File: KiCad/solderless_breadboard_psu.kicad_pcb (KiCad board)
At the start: 4 copper layers, 55 x 49.8 mm, 87 parts, among them IC301 MCP73831T-2ACI_OT, IC302 BQ29737DSER, IC401 TLV62569DBVR, IC501 FT232RL-REEL, J201 Barrel_Jack_Switch_Pin3Ring, J301 BM02B-GHS-TBT_LF__SN__N_, J501 Conn_01x09_Pin, J502 Conn_01x09_Pin, J503 Conn_01x06_Pin, J504 USB_C_Receptacle_USB2.0_16P, J601 Conn_02x03_Odd_Even, J602 Conn_02x03_Odd_Even, Q301 DMG3415U-7, Q302 T2N7002AK, Q303 T2N7002AK, U401 TPS61040DBVR, U501 USBLC6-2SC6

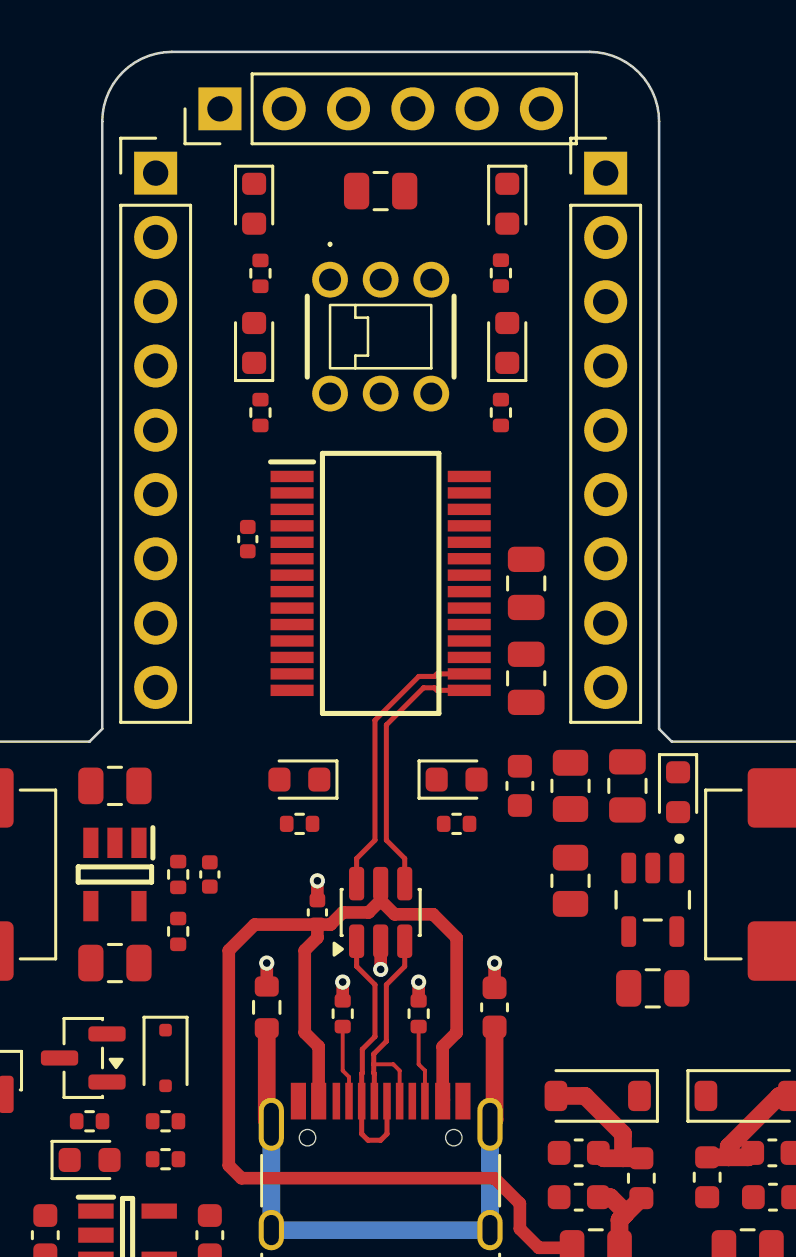
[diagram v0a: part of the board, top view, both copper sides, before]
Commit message: PCB UART routing
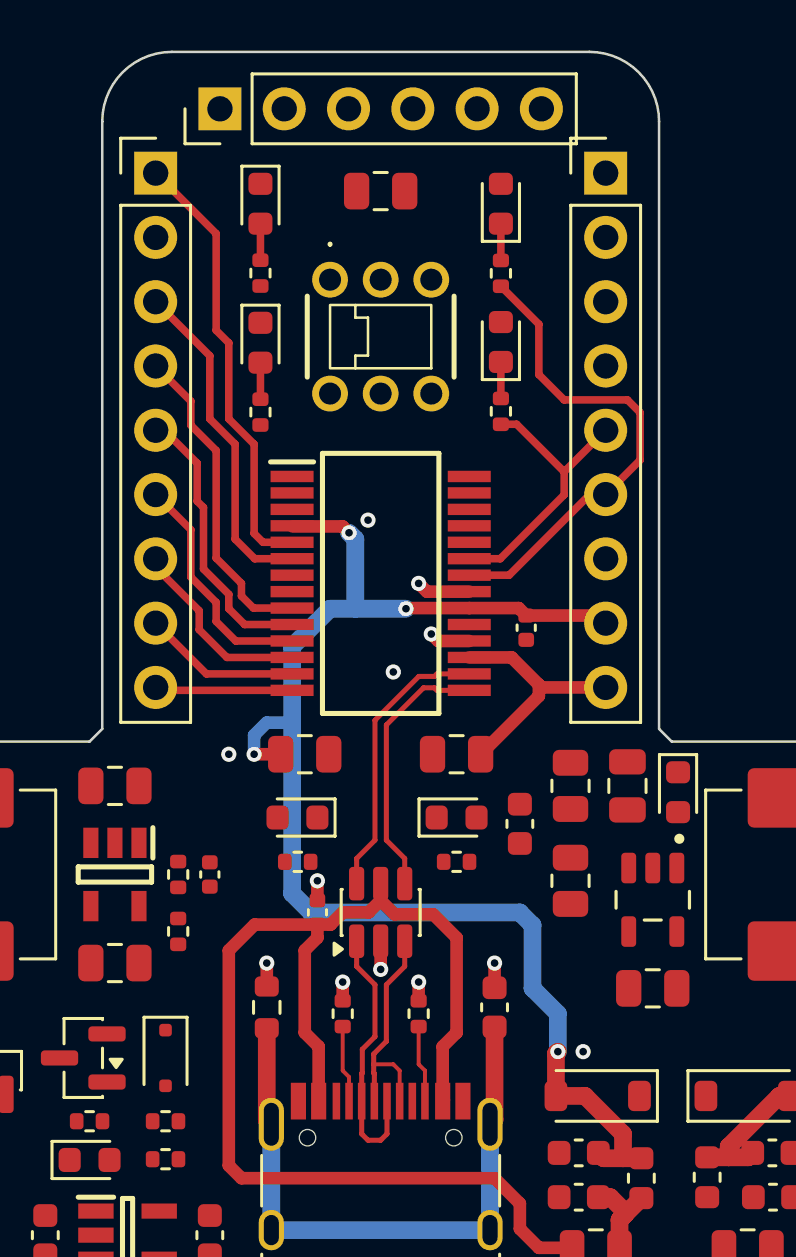
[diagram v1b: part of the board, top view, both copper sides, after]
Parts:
- moved C502 11.5 mm to (55.8, 70.5)
- moved C501 11.1 mm to (47.0, 75.5), turned to 0 degrees
- moved D501 9.75 mm to (54.8, 59.2)
- moved D606 9.75 mm to (45.2, 53.8)
- moved R503 9.50 mm to (54.8, 62.0)
- moved R606 9.50 mm to (45.2, 56.5)
- moved D502 5.51 mm to (54.8, 53.8)
- moved R504 5.50 mm to (54.8, 56.5)
- moved D605 5.50 mm to (45.2, 59.2)
- moved R605 5.48 mm to (45.2, 62.0)
- moved C503 4.07 mm to (53.0, 75.5), turned to 180 degrees
- moved D403 1.50 mm to (46.7, 78.0)
- moved R406 1.50 mm to (46.7, 79.8)
- moved C405 1.50 mm to (55.5, 78.2)
- moved D402 1.50 mm to (53.0, 78.0)
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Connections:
- J501 pad 5: /[5]USB 2 UART/RXD -> /[5]USB 2 UART/RX_LED
- J501 pad 6: /[5]USB 2 UART/RI -> /[5]USB 2 UART/TX_LED
- J501 pad 8: /[5]USB 2 UART/DSR -> +VCC_USB2UART_FILT
- J501 pad 9: /[5]USB 2 UART/DCD -> +3V3_FTDI
- J502 pad 1: /[5]USB 2 UART/RX_LED -> /[5]USB 2 UART/RXD
- J502 pad 3: /[5]USB 2 UART/TX_LED -> /[5]USB 2 UART/RI
- J502 pad 4: +VCC_USB2UART_FILT -> /[5]USB 2 UART/DSR
- J502 pad 5: +3V3_FTDI -> /[5]USB 2 UART/DCD
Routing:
- net +VCC_USB2UART_FILT: track 6.02 -> 55.4 mm, vias 0 -> 4
- net /[5]USB 2 UART/TX_LED: track 0.00 -> 19.2 mm
- net /[5]USB 2 UART/RXD: track 0.00 -> 17.5 mm
- net /[5]USB 2 UART/RI: track 0.00 -> 13.3 mm
- net /[5]USB 2 UART/DSR: track 0.00 -> 12.7 mm
- net /[5]USB 2 UART/RX_LED: track 0.00 -> 11.3 mm
- net /[5]USB 2 UART/DCD: track 0.00 -> 11.2 mm
- net +3V3_FTDI: track 0.00 -> 9.58 mm
- net /[5]USB 2 UART/CTS: track 0.00 -> 9.32 mm
- net /[5]USB 2 UART/SLEEP: track 0.00 -> 8.18 mm
- net /[5]USB 2 UART/TEN: track 0.00 -> 6.22 mm
- net /[5]USB 2 UART/PWREN: track 0.00 -> 5.44 mm
- net GND: track 5.26 -> 9.01 mm, vias 6 -> 12
- net Net-(D502-K): track 0.00 -> 1.45 mm
- net Net-(D501-K): track 0.00 -> 1.44 mm
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
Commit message: Update FTDI pinout
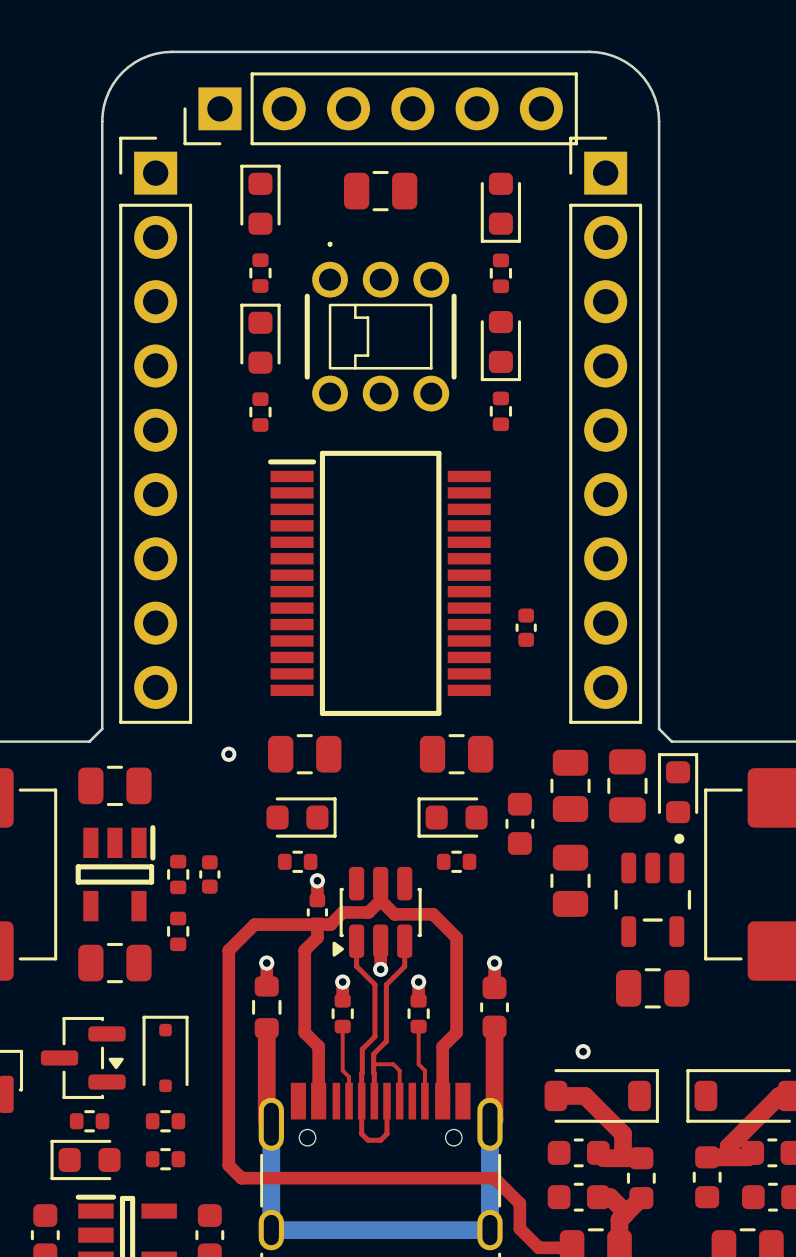
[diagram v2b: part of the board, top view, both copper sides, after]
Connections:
- J501 pad 1: /[5]USB 2 UART/TXD -> GND
- J501 pad 2: /[5]USB 2 UART/DTR -> +VCC_USB2UART_FILT
- J501 pad 3: /[5]USB 2 UART/RTS -> +3V3_FTDI
- J501 pad 4: VCC_FTDI -> GND
- J501 pad 5: /[5]USB 2 UART/RX_LED -> GND
- J501 pad 6: /[5]USB 2 UART/TX_LED -> /[5]USB 2 UART/CTS
- J501 pad 7: GND -> /[5]USB 2 UART/SLEEP
- J501 pad 8: +VCC_USB2UART_FILT -> /[5]USB 2 UART/TEN
- J501 pad 9: +3V3_FTDI -> /[5]USB 2 UART/PWREN
- J502 pad 1: /[5]USB 2 UART/RXD -> /[5]USB 2 UART/TXD
- J502 pad 2: GND -> /[5]USB 2 UART/DTR
- J502 pad 3: /[5]USB 2 UART/RI -> /[5]USB 2 UART/RTS
- J502 pad 4: /[5]USB 2 UART/DSR -> VCC_FTDI
- J502 pad 5: /[5]USB 2 UART/DCD -> /[5]USB 2 UART/RXD
- J502 pad 6: /[5]USB 2 UART/CTS -> /[5]USB 2 UART/RI
- J502 pad 7: /[5]USB 2 UART/SLEEP -> GND
- J502 pad 8: /[5]USB 2 UART/TEN -> /[5]USB 2 UART/DSR
- J502 pad 9: /[5]USB 2 UART/PWREN -> /[5]USB 2 UART/DCD
- J503 pad 1: /[5]USB 2 UART/DTR -> GND
- J503 pad 2: /[5]USB 2 UART/RXD -> /[5]USB 2 UART/CTS
- J503 pad 3: /[5]USB 2 UART/TXD -> VCC_FTDI
- J503 pad 4: VCC_FTDI -> /[5]USB 2 UART/TXD
- J503 pad 5: /[5]USB 2 UART/CTS -> /[5]USB 2 UART/RXD
- J503 pad 6: GND -> /[5]USB 2 UART/DTR
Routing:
- net +VCC_USB2UART_FILT: track 55.4 -> 6.02 mm, vias 4 -> 0
- net /[5]USB 2 UART/TX_LED: track 19.2 -> 0.00 mm
- net /[5]USB 2 UART/RXD: track 17.5 -> 0.00 mm
- net /[5]USB 2 UART/RI: track 13.3 -> 0.00 mm
- net /[5]USB 2 UART/DSR: track 12.7 -> 0.00 mm
- net /[5]USB 2 UART/RX_LED: track 11.3 -> 0.00 mm
- net /[5]USB 2 UART/USB2UART_D-: track 11.2 -> 0.00 mm
- net /[5]USB 2 UART/DCD: track 11.2 -> 0.00 mm
- net /[5]USB 2 UART/USB2UART_D+: track 10.5 -> 0.00 mm
- net +3V3_FTDI: track 9.58 -> 0.00 mm
- net /[5]USB 2 UART/CTS: track 9.32 -> 0.00 mm
- net /[5]USB 2 UART/SLEEP: track 8.18 -> 0.00 mm
- net /[5]USB 2 UART/TEN: track 6.22 -> 0.00 mm
- net /[5]USB 2 UART/PWREN: track 5.44 -> 0.00 mm
- net GND: track 9.01 -> 5.26 mm, vias 12 -> 8
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
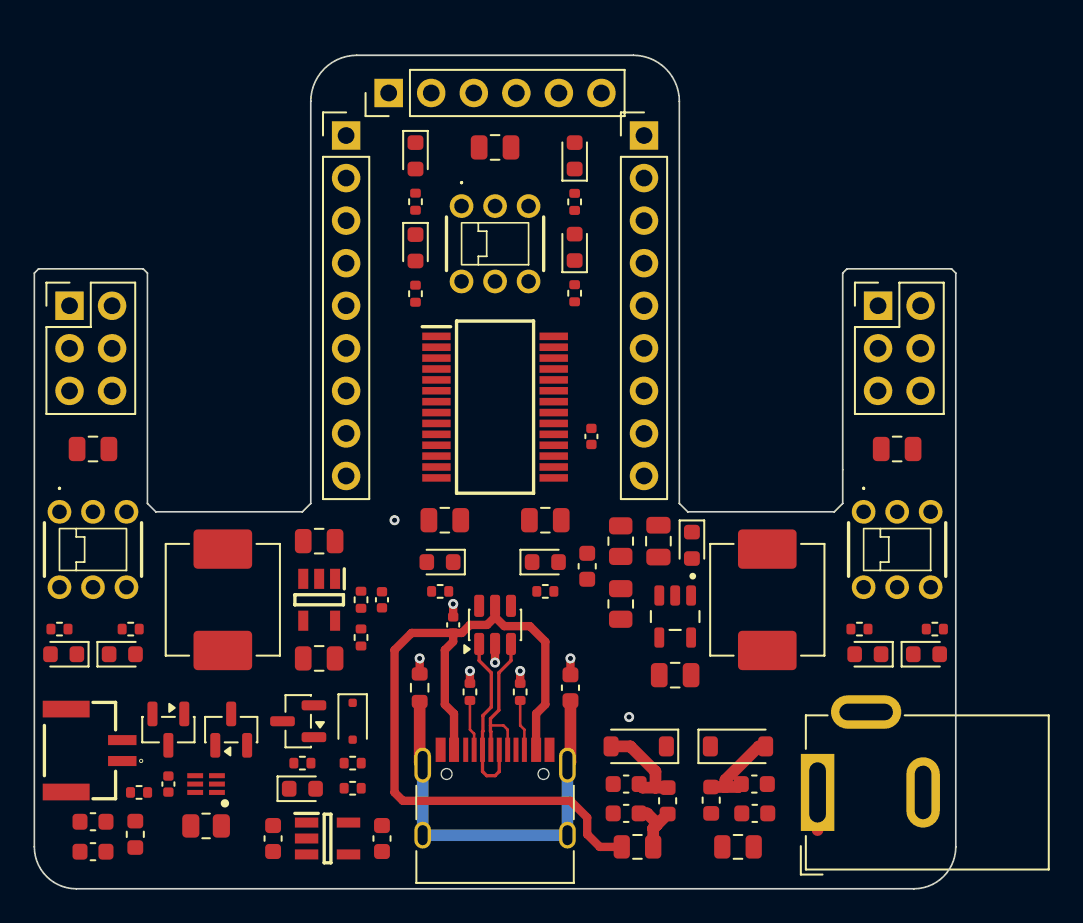
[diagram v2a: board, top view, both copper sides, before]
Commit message: FTDI signals routing
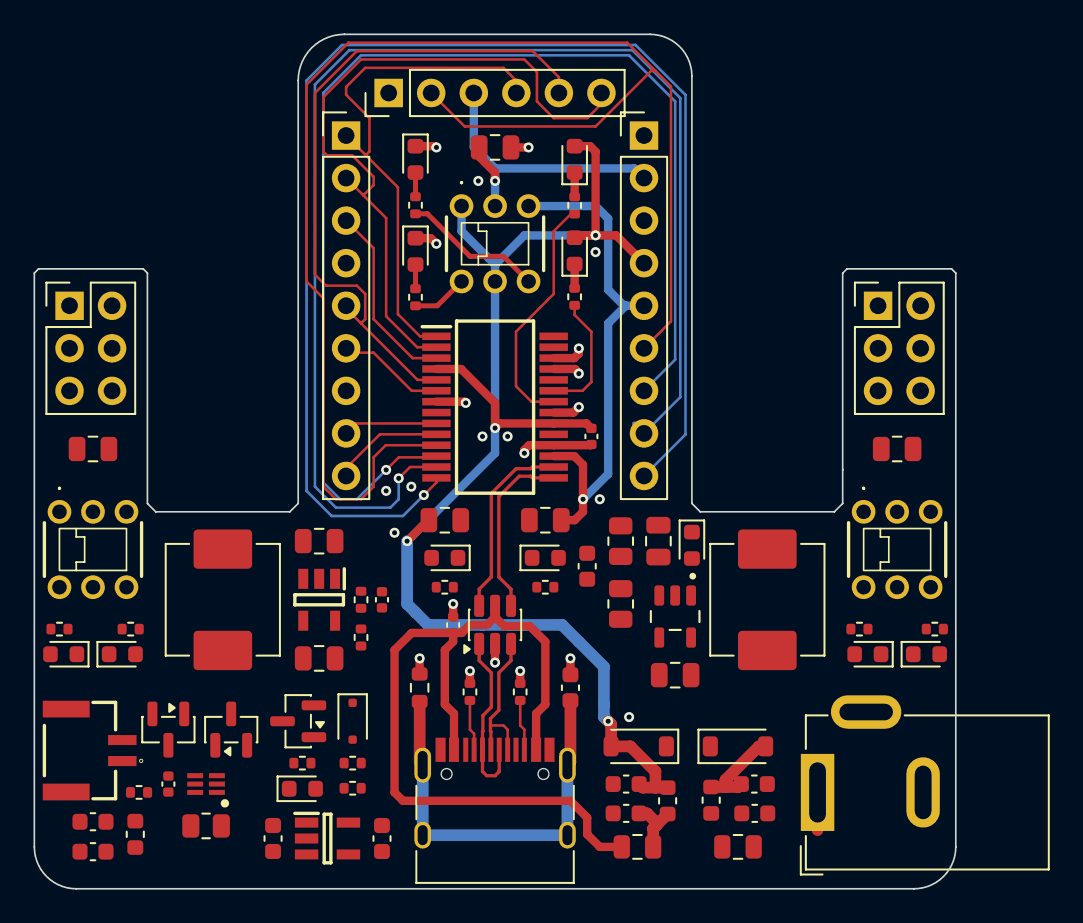
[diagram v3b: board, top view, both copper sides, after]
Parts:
- moved D403 0.38 mm to (47.0, 77.8)
- moved R406 0.37 mm to (47.0, 79.5), turned to 180 degrees
- moved D402 0.25 mm to (53.0, 77.8)
- moved R405 0.25 mm to (53.0, 79.5)
- moved D501 0.21 mm to (54.8, 59.4)
- moved D502 0.21 mm to (54.8, 54.0)
- moved D605 0.21 mm to (45.2, 59.5)
- moved D606 0.21 mm to (45.2, 54.0)
- moved R503 0.21 mm to (54.8, 62.2)
- moved R504 0.21 mm to (54.8, 56.7)
- moved R605 0.21 mm to (45.2, 62.2)
- moved R606 0.21 mm to (45.2, 56.7)
- turned C603 to 0 degrees
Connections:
- J501 pad 2: +VCC_USB2UART_FILT -> VCC_FTDI
- J501 pad 3: +3V3_FTDI -> GND
- J501 pad 4: GND -> +VCC_USB2UART_FILT
- J501 pad 5: GND -> +3V3_FTDI
- J502 pad 4: VCC_FTDI -> GND
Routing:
- net /[5]USB 2 UART/CTS: track 0.00 -> 89.6 mm
- net /[5]USB 2 UART/PWREN: track 0.00 -> 82.5 mm, vias 0 -> 1
- net /[5]USB 2 UART/TEN: track 0.00 -> 79.1 mm, vias 0 -> 1
- net +VCC_USB2UART_FILT: track 6.02 -> 82.9 mm, vias 0 -> 4
- net /[5]USB 2 UART/SLEEP: track 0.00 -> 72.6 mm, vias 0 -> 1
- net /[5]USB 2 UART/DTR: track 0.00 -> 42.2 mm
- net /[5]USB 2 UART/RXD: track 0.00 -> 40.7 mm
- net /[5]USB 2 UART/TXD: track 0.00 -> 31.3 mm
- net +3V3_FTDI: track 0.00 -> 30.7 mm, vias 0 -> 1
- net VCC_FTDI: track 0.00 -> 18.8 mm, vias 0 -> 1
- net GND: track 5.26 -> 20.3 mm, vias 8 -> 23
- net /[5]USB 2 UART/TX_LED: track 0.00 -> 14.5 mm
- net /[5]USB 2 UART/USB2UART_D-: track 0.00 -> 11.4 mm
- net /[5]USB 2 UART/RTS: track 0.00 -> 11.3 mm
- net /[5]USB 2 UART/USB2UART_D+: track 0.00 -> 10.6 mm
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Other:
- board size 55 x 49.8 mm -> 55 x 51 mm

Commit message: battery connector PCB routing
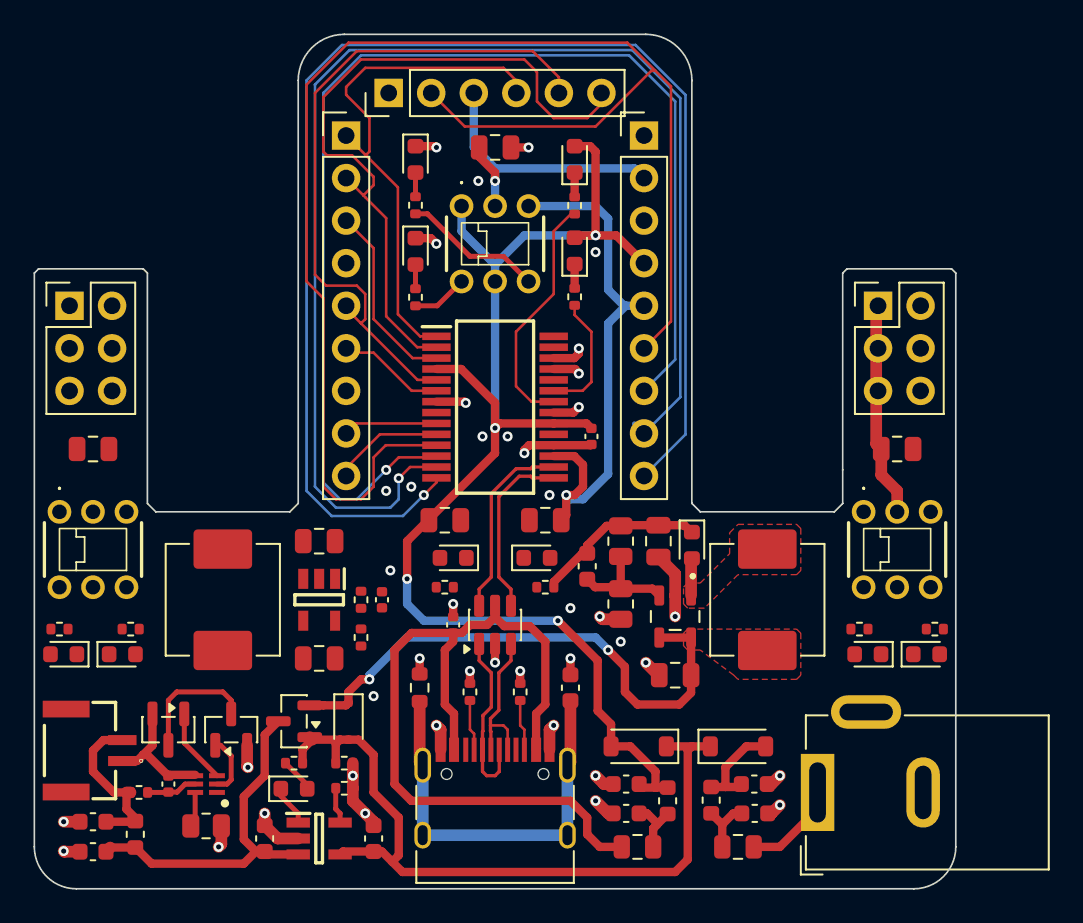
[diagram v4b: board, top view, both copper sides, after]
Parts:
- moved C301 0.50 mm to (42.8, 94.5)
- moved C302 0.50 mm to (36.2, 94.5)
- moved D302 0.50 mm to (38.0, 91.5)
- moved D402 0.50 mm to (52.5, 77.8)
- moved D403 0.50 mm to (47.5, 77.8)
- moved IC301 0.50 mm to (39.5, 94.5)
- moved R301 0.50 mm to (41.0, 90.0)
- moved R302 0.50 mm to (38.0, 90.0)
- moved R303 0.50 mm to (41.0, 91.5)
- moved D301 0.25 mm to (41.2, 87.5)
- moved Q301 0.25 mm to (38.0, 87.5)
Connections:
- S601 pad 5: +VIN_SWITCH -> +5V
- S602 pad 5: +VIN_SWITCH -> +5V
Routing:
- net +5V_IN: track 0.00 -> 45.7 mm
- net +VIN_SWITCH: track 0.00 -> 33.0 mm, vias 0 -> 2
- net GND: track 20.3 -> 46.2 mm, vias 23 -> 41
- net VBAT: track 0.00 -> 21.3 mm
- net VCC_R: track 0.00 -> 12.9 mm
- net +5V: track 0.00 -> 10.5 mm
- net CELL+: track 0.00 -> 9.71 mm
- net CELL-: track 0.00 -> 7.73 mm
- net Net-(Q302-D): track 0.00 -> 7.66 mm
- net /[4]Buck Boost converter/BST_FB_5V: track 0.00 -> 6.63 mm
- net /[3] Battery/DOUT: track 0.00 -> 4.50 mm
- net +5V_IN_FUSE: track 0.00 -> 3.71 mm
- net /[3] Battery/COUT: track 0.00 -> 3.60 mm
- net +5V_BJ: track 2.25 -> 5.74 mm
- net /[3] Battery/BAT: track 0.00 -> 3.05 mm
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- added copper zone on F.Cu, net +VIN_SWITCH
- added copper zone on F.Cu, net /[4]Buck Boost converter/BST_SW_5V
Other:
- outline, holes or cut-outs redrawn

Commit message: PCB route complete
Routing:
- net +5V: track 10.5 -> 97.9 mm, vias 0 -> 4
- net +3V3: track 0.00 -> 68.7 mm, vias 0 -> 1
- net GND: track 46.2 -> 65.1 mm, vias 41 -> 59
- net VCC_L: track 0.00 -> 12.9 mm
- net /[4]Buck Boost converter/BUCK_FB: track 0.00 -> 4.06 mm
- net Net-(R604-Pad2): track 0.00 -> 2.81 mm
- net Net-(R603-Pad2): track 0.00 -> 2.81 mm
- net Net-(R601-Pad2): track 0.00 -> 2.71 mm
- net Net-(R602-Pad2): track 0.00 -> 2.61 mm
- net Net-(D403-A): track 0.00 -> 2.08 mm
- net Net-(D402-A): track 0.00 -> 2.08 mm
- net Net-(D604-A): track 0.00 -> 1.83 mm
- net Net-(D603-A): track 0.00 -> 1.83 mm
- net Net-(D602-A): track 0.00 -> 1.59 mm
- net Net-(D601-A): track 0.00 -> 1.51 mm
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- added copper zone on F.Cu, net +3V3
- added copper zone on F.Cu, net /[4]Buck Boost converter/BUCK_SW
